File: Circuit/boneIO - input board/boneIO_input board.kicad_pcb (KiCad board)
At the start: 2 copper layers, 256 x 74 mm, 264 parts, among them J1 Screw_Terminal_01x08, J10 Screw_Terminal_01x08, J11 Screw_Terminal_01x08, J12 ZW_VCC, J13 ZW_GND, J14 INNY ZASILACZ, J15 BeagleBone_Black_Header, J16 BeagleBone_Black_Header, J2 Screw_Terminal_01x08, J3 Screw_Terminal_01x08, J4 Screw_Terminal_01x08, J5 Screw_Terminal_01x08, J6 Screw_Terminal_01x08, J7 Screw_Terminal_01x08, J8 Screw_Terminal_01x04, J9 Conn_02x04_Odd_Even, SW1 SW_Push, U1 P82B96, U10 LM2596S-ADJ, U11 RS485, U12 PC817X2NIP0F, U13 PC817X2NIP0F, U14 PC817X2NIP0F, U15 PC817X2NIP0F, U16 PC817X2NIP0F, U17 PC817X2NIP0F, U18 PC817X2NIP0F, U19 PC817X2NIP0F, U2 PC817X2NIP0F, U20 PC817X2NIP0F, U21 PC817X2NIP0F, U22 PC817X2NIP0F, U23 PC817X2NIP0F, U24 PC817X2NIP0F, U25 PC817X2NIP0F, U26 PC817X2NIP0F, U27 PC817X2NIP0F, U28 PC817X2NIP0F, U29 PC817X2NIP0F, U3 PC817X2NIP0F, U30 PC817X2NIP0F, U31 PC817X2NIP0F, U32 PC817X2NIP0F, U33 PC817X2NIP0F, U34 PC817X2NIP0F, U35 PC817X2NIP0F, U36 DS1307Z+, U37 PC817X2NIP0F, U38 PC817X2NIP0F, U39 PC817X2NIP0F, U4 PC817X2NIP0F, U40 PC817X2NIP0F, U41 PC817X2NIP0F, U42 PC817X2NIP0F, U43 PC817X2NIP0F, U44 PC817X2NIP0F, U45 PC817X2NIP0F, U46 PC817X2NIP0F, U47 PC817X2NIP0F, U48 PC817X2NIP0F, U49 PC817X2NIP0F, U5 PC817X2NIP0F, U50 PC817X2NIP0F, U51 PC817X2NIP0F, U52 PC817X2NIP0F, U53 PC817X2NIP0F, U54 PC817X2NIP0F, U55 PC817X2NIP0F, U56 PC817X2NIP0F, U6 PC817X2NIP0F, U7 PC817X2NIP0F, U8 PC817X2NIP0F, U9 PC817X2NIP0F, Y1 32,788 MHz

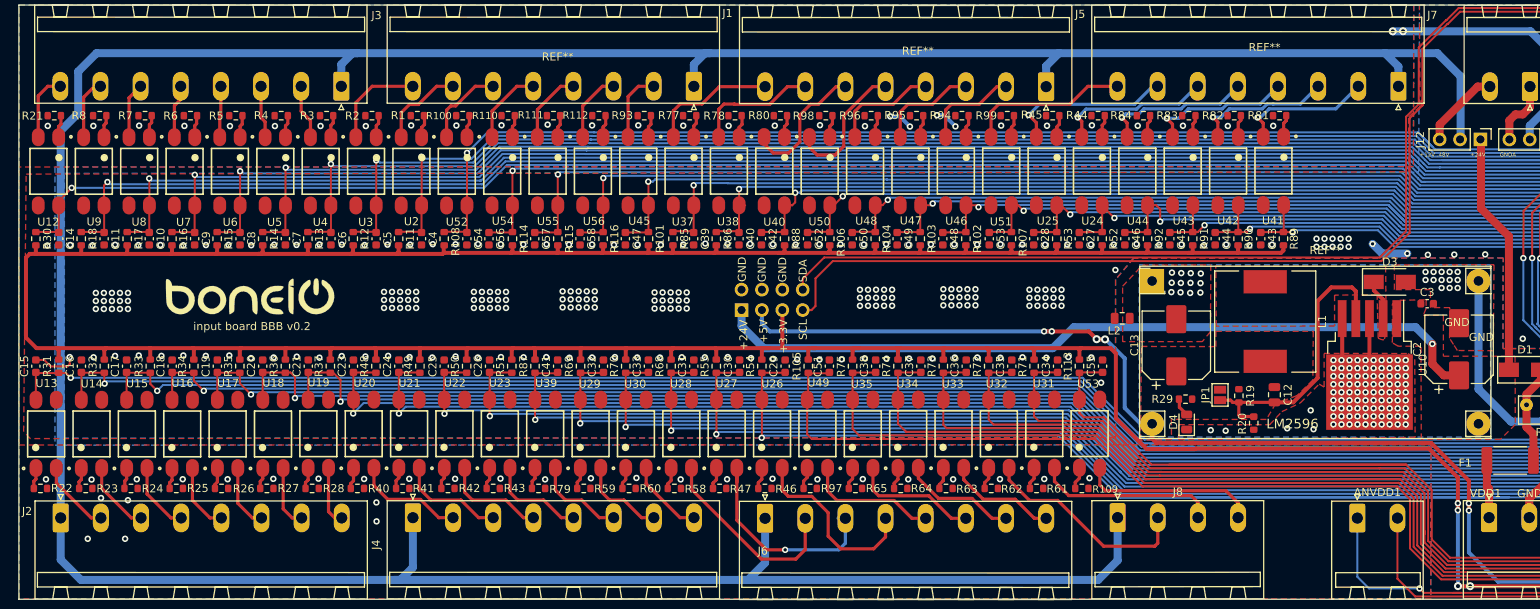
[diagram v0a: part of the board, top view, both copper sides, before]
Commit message: Correction of a schematic error and repair of 3d models
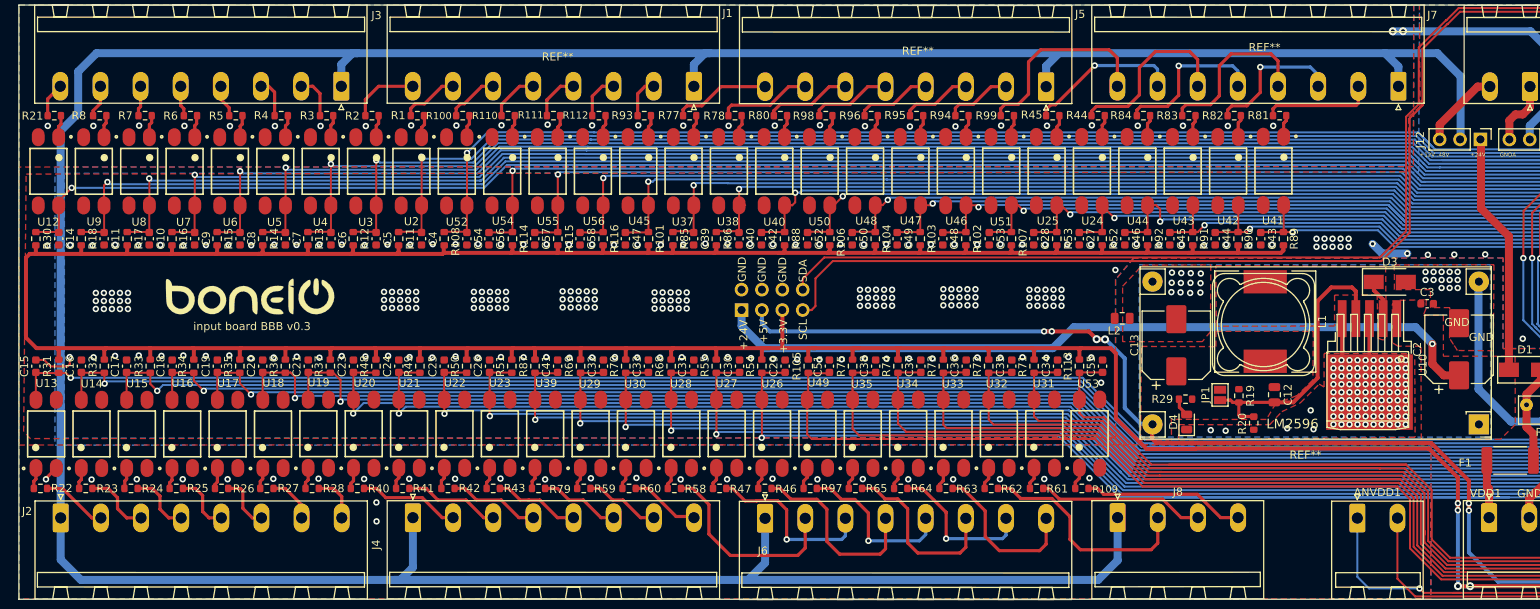
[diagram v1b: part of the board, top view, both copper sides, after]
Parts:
- removed the REF** at (160.8, 80.7)
- added REF**: YAAJ_DCDC_StepDown_LM2596, RF_Module:YAAJ_DCDC_StepDown_LM2596, F.Cu at (201.5, 98.5)
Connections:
- R1 pad 2: GNDA -> P8.45_OUT
- R100 pad 2: GNDA -> P8.46_OUT
- R109 pad 2: GNDA -> P8.07_OUT
- R110 pad 2: GNDA -> P9.42_OUT
- R111 pad 2: GNDA -> P9.31_OUT
- R112 pad 2: GNDA -> P9.30_OUT
- R2 pad 2: GNDA -> P8.44_OUT
- R21 pad 2: GNDA -> P8.37_OUT
- R22 pad 2: GNDA -> P8.36_OUT
- R23 pad 2: GNDA -> P8.35_OUT
- R24 pad 2: GNDA -> P8.34_OUT
- R25 pad 2: GNDA -> P8.33_OUT
- R26 pad 2: GNDA -> P8.32_OUT
- R27 pad 2: GNDA -> P8.31_OUT
- R28 pad 2: GNDA -> P8.30_OUT
- R3 pad 2: GNDA -> P8.43_OUT
- R4 pad 2: GNDA -> P8.42_OUT
- R40 pad 2: GNDA -> P8.29_OUT
- R41 pad 2: GNDA -> P8.28_OUT
- R42 pad 2: GNDA -> P8.27_OUT
- R43 pad 2: GNDA -> P8.26_OUT
- R44 pad 2: GNDA -> P9.15_OUT
- R45 pad 2: GNDA -> P9.16_OUT
- R46 pad 2: GNDA -> P8.14_OUT
- R47 pad 2: GNDA -> P8.15_OUT
- R5 pad 2: GNDA -> P8.41_OUT
- R58 pad 2: GNDA -> P8.16_OUT
- R59 pad 2: GNDA -> P8.18_OUT
- R6 pad 2: GNDA -> P8.40_OUT
- R60 pad 2: GNDA -> P8.17_OUT
- R61 pad 2: GNDA -> P8.08_OUT
- R62 pad 2: GNDA -> P8.09_OUT
- R63 pad 2: GNDA -> P8.10_OUT
- R64 pad 2: GNDA -> P8.11_OUT
- R65 pad 2: GNDA -> P8.12_OUT
- R7 pad 2: GNDA -> P8.39_OUT
- R77 pad 2: GNDA -> P9.28_OUT
- R78 pad 2: GNDA -> P9.27_OUT
- R79 pad 2: GNDA -> P8.19_OUT
- R8 pad 2: GNDA -> P8.38_OUT
- R80 pad 2: GNDA -> P9.25_OUT
- R81 pad 2: GNDA -> P9.11_OUT
- R82 pad 2: GNDA -> P9.12_OUT
- R83 pad 2: GNDA -> P9.13_OUT
- R84 pad 2: GNDA -> P9.14_OUT
- R93 pad 2: GNDA -> P9.29_OUT
- R94 pad 2: GNDA -> P9.18_OUT
- R95 pad 2: GNDA -> P9.21_OUT
- R96 pad 2: GNDA -> P9.22_OUT
- R97 pad 2: GNDA -> P8.13_OUT
- R98 pad 2: GNDA -> P9.23_OUT
- R99 pad 2: GNDA -> P9.17_OUT
- U12 pad 2: P8.37_OUT -> GNDA
- U13 pad 2: P8.36_OUT -> GNDA
- U14 pad 2: P8.35_OUT -> GNDA
- U15 pad 2: P8.34_OUT -> GNDA
- U16 pad 2: P8.33_OUT -> GNDA
- U17 pad 2: P8.32_OUT -> GNDA
- U18 pad 2: P8.31_OUT -> GNDA
- U19 pad 2: P8.30_OUT -> GNDA
- U2 pad 2: P8.45_OUT -> GNDA
- U20 pad 2: P8.29_OUT -> GNDA
- U21 pad 2: P8.28_OUT -> GNDA
- U22 pad 2: P8.27_OUT -> GNDA
- U23 pad 2: P8.26_OUT -> GNDA
- U24 pad 2: P9.15_OUT -> GNDA
- U25 pad 2: P9.16_OUT -> GNDA
- U26 pad 2: P8.14_OUT -> GNDA
- U27 pad 2: P8.15_OUT -> GNDA
- U28 pad 2: P8.16_OUT -> GNDA
- U29 pad 2: P8.18_OUT -> GNDA
- U3 pad 2: P8.44_OUT -> GNDA
- U30 pad 2: P8.17_OUT -> GNDA
- U31 pad 2: P8.08_OUT -> GNDA
- U32 pad 2: P8.09_OUT -> GNDA
- U33 pad 2: P8.10_OUT -> GNDA
- U34 pad 2: P8.11_OUT -> GNDA
- U35 pad 2: P8.12_OUT -> GNDA
- U37 pad 2: P9.28_OUT -> GNDA
- U38 pad 2: P9.27_OUT -> GNDA
- U39 pad 2: P8.19_OUT -> GNDA
- U4 pad 2: P8.43_OUT -> GNDA
- U40 pad 2: P9.25_OUT -> GNDA
- U41 pad 2: P9.11_OUT -> GNDA
- U42 pad 2: P9.12_OUT -> GNDA
- U43 pad 2: P9.13_OUT -> GNDA
- U44 pad 2: P9.14_OUT -> GNDA
- U45 pad 2: P9.29_OUT -> GNDA
- U46 pad 2: P9.18_OUT -> GNDA
- U47 pad 2: P9.21_OUT -> GNDA
- U48 pad 2: P9.22_OUT -> GNDA
- U49 pad 2: P8.13_OUT -> GNDA
- U5 pad 2: P8.42_OUT -> GNDA
- U50 pad 2: P9.23_OUT -> GNDA
- U51 pad 2: P9.17_OUT -> GNDA
- U52 pad 2: P8.46_OUT -> GNDA
- U53 pad 2: P8.07_OUT -> GNDA
- U54 pad 2: P9.42_OUT -> GNDA
- U55 pad 2: P9.31_OUT -> GNDA
- U56 pad 2: P9.30_OUT -> GNDA
- U6 pad 2: P8.41_OUT -> GNDA
- U7 pad 2: P8.40_OUT -> GNDA
- U8 pad 2: P8.39_OUT -> GNDA
- U9 pad 2: P8.38_OUT -> GNDA
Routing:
- net P8.12_OUT: track 15.8 -> 22.6 mm
- net P9.23_OUT: track 16.9 -> 10.2 mm
- net P8.10_OUT: track 13.7 -> 20.3 mm
- net P9.25_OUT: track 17.5 -> 11.4 mm
- net P8.15_OUT: track 27.9 -> 22.0 mm
- net P8.11_OUT: track 14.3 -> 19.1 mm, vias 0 -> 1
- net P9.17_OUT: track 20.2 -> 24.7 mm
- net P8.13_OUT: track 16.5 -> 20.6 mm, vias 0 -> 1
- net P8.37_OUT: track 8.38 -> 4.31 mm
- net P9.22_OUT: track 13.3 -> 9.48 mm
- net P9.27_OUT: track 16.0 -> 12.2 mm
- net P9.28_OUT: track 15.9 -> 12.2 mm
- net P8.45_OUT: track 11.0 -> 7.29 mm
- net P9.21_OUT: track 12.6 -> 8.84 mm
- net P8.46_OUT: track 10.4 -> 6.65 mm
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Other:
- board text added: "input board BBB v0.3"
- board text removed: "input board BBB v0.2"

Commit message: relay board v0.3 and some cleanup
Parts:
- removed the J12 at (201.7, 63.0)
- removed the J13 at (210.3, 63.0)
- removed the J14 at (207.8, 56.5)
- removed the R108 at (72.6, 75.4)
- removed the R11 at (66.9, 75.4)
- removed the U11 at (240.6, 59.4)
- added C38: 100n, Capacitor_SMD:C_0603_1608Metric, F.Cu at (245.4, 85.6)
- added J4: ZASILACZ, Connector_Phoenix_MSTB:PhoenixContact_MSTBA_2,5_2-G_1x02_P5.00mm_Horizontal, F.Cu at (207.8, 56.4)
- added L3: BLM21PG221SN1D, Inductor_SMD:L_0805_2012Metric, F.Cu at (196.8, 56.9)
- added L4: BLM21PG221SN1D, Inductor_SMD:L_0805_2012Metric, F.Cu at (196.8, 50.3)
- added Q1: BSS138, Package_TO_SOT_SMD:SOT-23, F.Cu at (233.9, 74.9)
- added Q2: BSS138, Package_TO_SOT_SMD:SOT-23, F.Cu at (233.8, 79.8)
- added R103: 10k, Resistor_SMD:R_0603_1608Metric, F.Cu at (213.8, 53.1)
- added R104: 10k, Resistor_SMD:R_0603_1608Metric, F.Cu at (213.8, 54.9)
- added R109: 10k, Resistor_SMD:R_0603_1608Metric, F.Cu at (188.2, 74.0)
- added R110: 10k, Resistor_SMD:R_0603_1608Metric, F.Cu at (213.8, 51.5)
- added R111: 10k, Resistor_SMD:R_0603_1608Metric, F.Cu at (195.1, 74.0)
- added R112: 10k, Resistor_SMD:R_0603_1608Metric, F.Cu at (213.8, 56.6)
- added R121: 4.7k, Resistor_SMD:R_0603_1608Metric, F.Cu at (239.7, 74.8)
- added R122: 4.7k, Resistor_SMD:R_0603_1608Metric, F.Cu at (239.7, 80.0)
- added R123: 4.7k, Resistor_SMD:R_0603_1608Metric, F.Cu at (236.8, 74.8)
- added R124: 4.7k, Resistor_SMD:R_0603_1608Metric, F.Cu at (236.8, 79.7)
- added R125: 4.7k, Resistor_SMD:R_0603_1608Metric, F.Cu at (230.2, 75.0)
- added R126: 4.7k, Resistor_SMD:R_0603_1608Metric, F.Cu at (230.2, 79.7)
- added U51: PC817X2NIP0F, PC817:SOT254P975X400-4N, F.Cu at (182.0, 66.9)
- added U52: PC817X2NIP0F, PC817:SOT254P975X400-4N, F.Cu at (188.3, 66.9)
- added U57: PC817X2NIP0F, PC817:SOT254P975X400-4N, F.Cu at (194.5, 66.9)
- added U58: PC817X2NIP0F, PC817:SOT254P975X400-4N, F.Cu at (200.5, 66.9)
- added U59: PC817X2NIP0F, PC817:SOT254P975X400-4N, F.Cu at (206.5, 66.9)
- added U60: PC817X2NIP0F, PC817:SOT254P975X400-4N, F.Cu at (212.7, 66.9)
- added U61: RS485, rs485:RS485_moduleTTL, B.Cu at (240.2, 59.4)
- I2C1: value Conn_01x04 -> OLED
- R68: renamed from R66; value 10k -> 4.7k
- R69: renamed from R67; value 10k -> 4.7k
- U1: renamed from U52; footprint boneIO - RM85:SOT254P975X400-4N -> PC817:SOT254P975X400-4N
- U10: renamed from U9; footprint boneIO - RM85:SOT254P975X400-4N -> PC817:SOT254P975X400-4N
- U11: renamed from U12; footprint boneIO - RM85:SOT254P975X400-4N -> PC817:SOT254P975X400-4N
- U12: renamed from U13; footprint boneIO - RM85:SOT254P975X400-4N -> PC817:SOT254P975X400-4N
- U13: renamed from U14; footprint boneIO - RM85:SOT254P975X400-4N -> PC817:SOT254P975X400-4N
- U14: renamed from U15; footprint boneIO - RM85:SOT254P975X400-4N -> PC817:SOT254P975X400-4N
- U15: renamed from U16; footprint boneIO - RM85:SOT254P975X400-4N -> PC817:SOT254P975X400-4N
- U16: renamed from U17; footprint boneIO - RM85:SOT254P975X400-4N -> PC817:SOT254P975X400-4N
- U17: renamed from U18; footprint boneIO - RM85:SOT254P975X400-4N -> PC817:SOT254P975X400-4N
- U18: renamed from U39; footprint boneIO - RM85:SOT254P975X400-4N -> PC817:SOT254P975X400-4N
- U19: renamed from U29; footprint boneIO - RM85:SOT254P975X400-4N -> PC817:SOT254P975X400-4N
- U2, U27, U3, U4, U5, U55, U6, U7, U8: footprint boneIO - RM85:SOT254P975X400-4N -> PC817:SOT254P975X400-4N
- U20: renamed from U30; footprint boneIO - RM85:SOT254P975X400-4N -> PC817:SOT254P975X400-4N
- U21: renamed from U19; footprint boneIO - RM85:SOT254P975X400-4N -> PC817:SOT254P975X400-4N
- U22: renamed from U20; footprint boneIO - RM85:SOT254P975X400-4N -> PC817:SOT254P975X400-4N
- U23: renamed from U21; footprint boneIO - RM85:SOT254P975X400-4N -> PC817:SOT254P975X400-4N
- U24: renamed from U22; footprint boneIO - RM85:SOT254P975X400-4N -> PC817:SOT254P975X400-4N
- U25: renamed from U23; footprint boneIO - RM85:SOT254P975X400-4N -> PC817:SOT254P975X400-4N
- U26: renamed from U28; footprint boneIO - RM85:SOT254P975X400-4N -> PC817:SOT254P975X400-4N
- U28: renamed from U26; footprint boneIO - RM85:SOT254P975X400-4N -> PC817:SOT254P975X400-4N
- U29: renamed from U49; footprint boneIO - RM85:SOT254P975X400-4N -> PC817:SOT254P975X400-4N
- U30: renamed from U35; footprint boneIO - RM85:SOT254P975X400-4N -> PC817:SOT254P975X400-4N
- U31: renamed from U34; footprint boneIO - RM85:SOT254P975X400-4N -> PC817:SOT254P975X400-4N
- U32: renamed from U33; footprint boneIO - RM85:SOT254P975X400-4N -> PC817:SOT254P975X400-4N
- U33: renamed from U32; footprint boneIO - RM85:SOT254P975X400-4N -> PC817:SOT254P975X400-4N
- U35: renamed from U31; footprint boneIO - RM85:SOT254P975X400-4N -> PC817:SOT254P975X400-4N
- U36: renamed from U53; footprint boneIO - RM85:SOT254P975X400-4N -> PC817:SOT254P975X400-4N
- U37: renamed from U41; footprint boneIO - RM85:SOT254P975X400-4N -> PC817:SOT254P975X400-4N
- U38: renamed from U42; footprint boneIO - RM85:SOT254P975X400-4N -> PC817:SOT254P975X400-4N
- U39: renamed from U43; footprint boneIO - RM85:SOT254P975X400-4N -> PC817:SOT254P975X400-4N
- U40: renamed from U44; footprint boneIO - RM85:SOT254P975X400-4N -> PC817:SOT254P975X400-4N
- U41: renamed from U24; footprint boneIO - RM85:SOT254P975X400-4N -> PC817:SOT254P975X400-4N
- U42: renamed from U25; footprint boneIO - RM85:SOT254P975X400-4N -> PC817:SOT254P975X400-4N
- U43: renamed from U51; footprint boneIO - RM85:SOT254P975X400-4N -> PC817:SOT254P975X400-4N
- U44: renamed from U46; footprint boneIO - RM85:SOT254P975X400-4N -> PC817:SOT254P975X400-4N
- U45: renamed from U47; footprint boneIO - RM85:SOT254P975X400-4N -> PC817:SOT254P975X400-4N
- U46: renamed from U48; footprint boneIO - RM85:SOT254P975X400-4N -> PC817:SOT254P975X400-4N
- U47: renamed from U50; footprint boneIO - RM85:SOT254P975X400-4N -> PC817:SOT254P975X400-4N
- U48: renamed from U40; footprint boneIO - RM85:SOT254P975X400-4N -> PC817:SOT254P975X400-4N
- U49: renamed from U38; footprint boneIO - RM85:SOT254P975X400-4N -> PC817:SOT254P975X400-4N
- U50: renamed from U37; footprint boneIO - RM85:SOT254P975X400-4N -> PC817:SOT254P975X400-4N
- U53: renamed from U45; footprint boneIO - RM85:SOT254P975X400-4N -> PC817:SOT254P975X400-4N
- U54: renamed from U56; footprint boneIO - RM85:SOT254P975X400-4N -> PC817:SOT254P975X400-4N
- U56: renamed from U54; footprint boneIO - RM85:SOT254P975X400-4N -> PC817:SOT254P975X400-4N
- moved R42 16.0 mm to (251.7, 86.3), turned to 180 degrees
- moved R69 15.9 mm to (240.8, 92.7), turned to 90 degrees
- moved R68 15.8 mm to (237.9, 92.7), turned to 90 degrees
- moved BT1 14.1 mm to (239.5, 97.0), turned to 180 degrees
- moved R51 14.0 mm to (251.7, 83.8), turned to 0 degrees
- moved C29 11.4 mm to (252.7, 77.6), turned to 180 degrees
- moved R78 11.3 mm to (243.7, 92.7), turned to 270 degrees
- moved D4 10.7 mm to (252.8, 80.7), turned to 0 degrees
- moved Y1 6.37 mm to (232.5, 86.0)
- moved U34 5.52 mm to (240.0, 86.8), turned to 0 degrees
- moved R117 4.80 mm to (237.6, 61.2), turned to 90 degrees
- moved R118 4.78 mm to (235.0, 61.2), turned to 90 degrees
- moved R99 3.01 mm to (117.6, 75.4)
- moved C17 2.96 mm to (36.0, 91.3)
- moved R30 2.95 mm to (33.1, 91.3)
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- renumbered C2 to C1, C12 to C11, C13 to C12, C11 to C13, C3 to C2, C41 to C21, C32 to C22, C33 to C23, C21 to C24, C23 to C25, C24 to C26, C25 to C27, C26 to C28, C22 to C29, C54 to C3, C31 to C30, C30 to C31, C29 to C32, C51 to C33, C38 to C34, C37 to C35, C35 to C37, C34 to C39, C55 to C40, C43 to C41, C44 to C42, C45 to C43, C46 to C44, C27 to C45, C28 to C46, C53 to C47, C52 to C51, C42 to C52, C40 to C53, C39 to C54, C47 to C55, C58 to C56, C56 to C58, C1 to C59, D3 to D2, D4 to D3, D5 to D4, D2 to D5, J11 to J1, J8 to J10, J15 to J11, J16 to J12, J9 to J13, J10 to J14, J1 to J2, J2 to J3, J3 to J5, J4 to J6, J5 to J7, J6 to J8, J7 to J9, R100 to R1, R13 to R10, R88 to R100, R86 to R101, R85 to R102, R93 to R105, R112 to R106, R111 to R107, R110 to R108, R14 to R11, R101 to R113, R116 to R114, R114 to R116, R56 to R117, R57 to R118, R9 to R119, R15 to R12, R10 to R120, R16 to R13, R17 to R14, R8 to R15, R21 to R16, R22 to R17, R23 to R18, R24 to R19, R1 to R2, R25 to R20, R26 to R21, R27 to R22, R19 to R23, R20 to R24, R29 to R25, R18 to R26, R30 to R27, R31 to R28, R32 to R29, R2 to R3, R33 to R30, R34 to R31, R35 to R32, R36 to R33, R79 to R34, R59 to R35, R60 to R36, R28 to R37, R40 to R38, R41 to R39, R3 to R4, R42 to R40, R43 to R41, R38 to R42, R87 to R43, R69 to R44, R70 to R45, R37 to R46, R48 to R47, R49 to R48, R50 to R49, R4 to R5, R51 to R50, R39 to R51, R58 to R52, R47 to R53, R46 to R54, R97 to R55, R65 to R56, R64 to R57, R63 to R58, R62 to R59, R5 to R6, R68 to R60, R55 to R61, R54 to R62, R105 to R63, R75 to R64, R74 to R65, R73 to R66, R72 to R67, R6 to R7, R61 to R70, R109 to R71, R81 to R72, R82 to R73, R83 to R74, R84 to R75, R44 to R76, R45 to R77, R76 to R78, R71 to R79, R7 to R8, R113 to R80, R89 to R81, R90 to R82, R91 to R83, R92 to R84, R52 to R85, R53 to R86, R99 to R87, R94 to R88, R95 to R89, R12 to R9, R96 to R90, R98 to R91, R80 to R92, R78 to R93, R77 to R94, R107 to R95, R102 to R96, R103 to R97, R104 to R98, R106 to R99, U36 to U34, U1 to U62, U10 to U9
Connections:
- net P8.03 renamed Net-(J12-Pad3)
- net P8.04 renamed Net-(J12-Pad4)
- net P8.05 renamed Net-(J12-Pad5)
- net P8.06 renamed Net-(J12-Pad6)
- net P8.20 renamed Net-(J12-Pad20)
- net P8.21 renamed Net-(J12-Pad21)
- net P8.22 renamed Net-(J12-Pad22)
- net P8.23 renamed Net-(J12-Pad23)
- net P8.24 renamed Net-(J12-Pad24)
- net P8.25 renamed Net-(J12-Pad25)
- R68 pad 1: +3V3 -> +5V
- R68 pad 2: SDA -> SDA_5V
- R69 pad 1: +3V3 -> +5V
- R69 pad 2: SCL -> SCL_5V
- R78 pad 1: +3V3 -> +5V
- U34 pad 5: SDA -> SDA_5V
- U34 pad 6: SCL -> SCL_5V
- U34 pad 8: +3V3 -> +5V
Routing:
- net +5V: track 217.8 -> 284.4 mm, vias 6 -> 8
- net P9.12: track 142.2 -> 193.3 mm
- net Net-(R110-Pad2): track 0.00 -> 48.5 mm
- net Net-(L4-Pad1): track 0.00 -> 41.5 mm, vias 0 -> 5
- net GND1: track 8.29 -> 47.0 mm
- net Net-(R103-Pad2): track 0.00 -> 35.1 mm
- net SDA_5V: track 0.00 -> 29.8 mm, vias 0 -> 2
- net SCL_5V: track 0.00 -> 27.1 mm
- net GNDA: track 36.4 -> 10.2 mm, vias 56 -> 57
- net +48V: track 10.0 -> 35.4 mm, vias 0 -> 3
- net +24V: track 127.7 -> 151.8 mm
- net Net-(L3-Pad1): track 0.00 -> 22.7 mm, vias 0 -> 2
- net Net-(R111-Pad2): track 0.00 -> 22.0 mm
- net Net-(R104-Pad2): track 0.00 -> 19.4 mm
- net SDA: track 227.8 -> 244.7 mm
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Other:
- board text added: "LAN/BBB"
- board text added: "Logic Level Converter"
- board text added: "WARNING!!!"
- board text removed: "+12V..48V"
- board text removed: "GNDA"
